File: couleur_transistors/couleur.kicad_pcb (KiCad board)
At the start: 2 copper layers, 13.7 x 33.5 mm, 12 parts, among them P1 CONN_02X03, P2 Mounting, U1 S4282-51

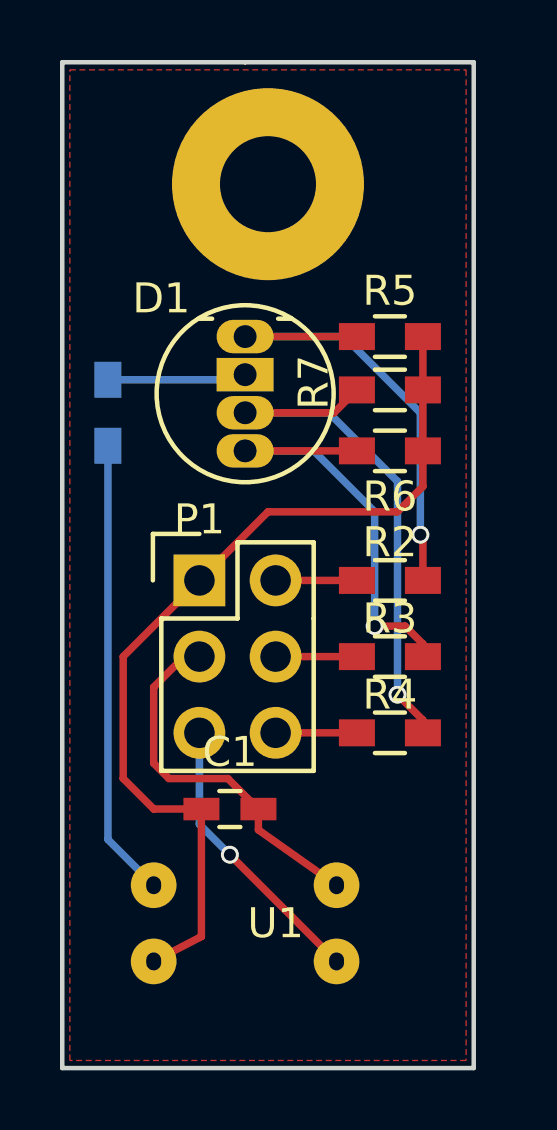
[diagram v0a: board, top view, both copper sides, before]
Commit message: COuleur avec transistors
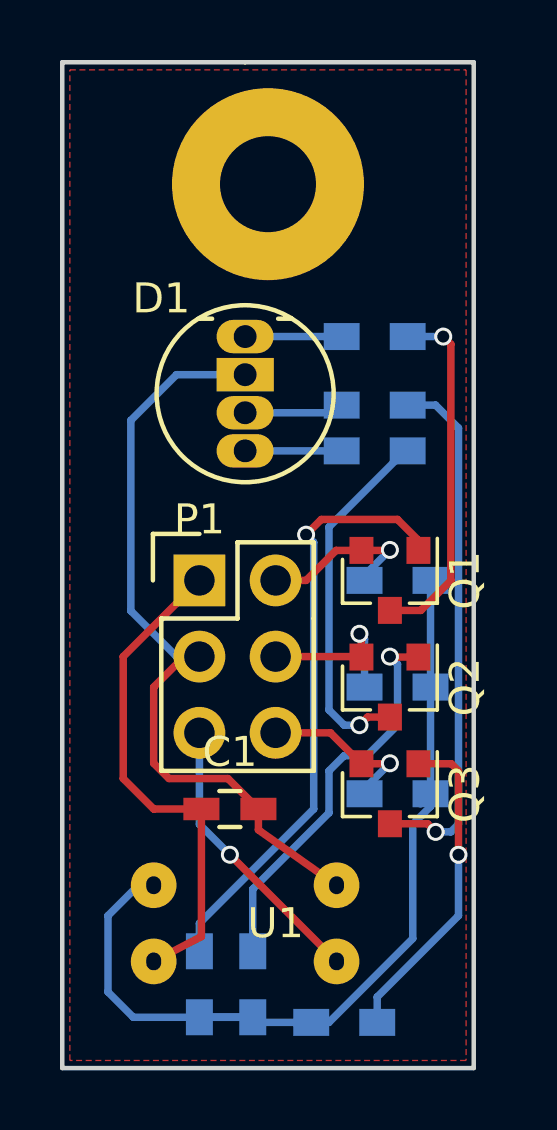
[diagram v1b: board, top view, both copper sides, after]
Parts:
- added Q1: Q_PNP_BEC, TO_SOT_Packages_SMD:SOT-23, F.Cu at (182.1, 104.1)
- added Q2: Q_PNP_BEC, TO_SOT_Packages_SMD:SOT-23, F.Cu at (182.1, 107.7)
- added Q3: Q_PNP_BEC, TO_SOT_Packages_SMD:SOT-23, F.Cu at (182.1, 111.3)
- added R8: 100, Resistors_SMD:R_0603_HandSoldering, B.Cu at (182.4, 111.3)
- added R9: 20, Resistors_SMD:R_0603_HandSoldering, B.Cu at (181.6, 98.3)
- R1: value R -> 0
- R2: value 150 -> 100; moved to B.Cu
- R3: value 76 -> 20; moved to B.Cu
- R4: value 82 -> 0; moved to B.Cu
- R5: value 600 -> 100; moved to B.Cu
- R6: value 122 -> 20; moved to B.Cu
- R7: value 131 -> 0; moved to B.Cu
- moved R7 21.1 mm to (180.6, 118.9), turned to 180 degrees
- moved R1 19.3 mm to (175.8, 117.6)
- moved R5 11.7 mm to (182.4, 107.7), turned to 180 degrees
- moved R3 10.7 mm to (181.6, 96.0), turned to 180 degrees
- moved R4 9.55 mm to (177.5, 117.6), turned to 270 degrees
- moved R6 0.51 mm to (181.6, 99.8), turned to 180 degrees
- moved R2 0.25 mm to (182.4, 104.1), turned to 180 degrees
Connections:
- D1 pad 2: Net-(D1-Pad2) -> GND
- R1 pad 1: Net-(D1-Pad2) -> Net-(Q1-Pad1)
- R1 pad 2: Net-(R1-Pad2) -> CATH
- R2 pad 1: RED -> CATH
- R2 pad 2: Net-(D1-Pad1) -> RED
- R3 pad 1: GREEN -> Net-(Q1-Pad3)
- R3 pad 2: Net-(D1-Pad4) -> Net-(D1-Pad1)
- R4 pad 1: BLUE -> Net-(Q2-Pad1)
- R4 pad 2: Net-(D1-Pad3) -> CATH
- R5 pad 1: Net-(D1-Pad1) -> CATH
- R5 pad 2: +5VL -> GREEN
- R6 pad 1: Net-(D1-Pad4) -> Net-(Q2-Pad3)
- R6 pad 2: +5VL -> Net-(D1-Pad4)
- R7 pad 1: Net-(D1-Pad3) -> Net-(Q3-Pad1)
- R7 pad 2: +5VL -> CATH
- U1 pad 1: Net-(R1-Pad2) -> CATH
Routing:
- net CATH: track 0.00 -> 31.3 mm
- net Net-(Q1-Pad1): track 0.00 -> 20.1 mm, vias 0 -> 1
- net Net-(Q3-Pad3): track 0.00 -> 17.7 mm, vias 0 -> 1
- net Net-(D1-Pad3): track 18.8 -> 3.32 mm, vias 1 -> 0
- net Net-(R1-Pad2): track 15.3 -> 0.00 mm
- net +5VL: track 30.5 -> 16.7 mm
- net GND: track 12.5 -> 26.2 mm
- net Net-(Q2-Pad1): track 0.00 -> 13.3 mm, vias 0 -> 1
- net Net-(D1-Pad1): track 16.2 -> 3.22 mm, vias 1 -> 0
- net Net-(Q2-Pad3): track 0.00 -> 12.1 mm, vias 0 -> 1
- net Net-(Q1-Pad3): track 0.00 -> 11.9 mm, vias 0 -> 1
- net Net-(D1-Pad4): track 15.2 -> 3.47 mm, vias 1 -> 0
- net Net-(Q3-Pad1): track 0.00 -> 10.9 mm, vias 0 -> 1
- net Net-(D1-Pad2): track 4.88 -> 0.00 mm
- net RED: track 2.79 -> 5.85 mm, vias 0 -> 1
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
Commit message: Couleur
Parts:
- removed Q2, Q3: Q_PNP_BEC, TO_SOT_Packages_SMD:SOT-23
- removed R1, R4, R7: 0, Resistors_SMD:R_0603_HandSoldering
- removed R2, R5, R8: 100, Resistors_SMD:R_0603_HandSoldering
- R3, R6, R9: moved to F.Cu
- moved Q1 7.41 mm to (182.2, 111.5), turned to 180 degrees
- moved R6 1.61 mm to (182.3, 101.2)
- moved R9 0.77 mm to (182.3, 98.5)
- moved R3 0.74 mm to (182.3, 96.0)
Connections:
- D1 pad 2: GND -> Net-(D1-Pad2)
- Q1 pad 1: Net-(Q1-Pad1) -> CATH
- Q1 pad 2: RED -> Net-(D1-Pad2)
- Q1 pad 3: Net-(Q1-Pad3) -> GND
- R3 pad 1: Net-(Q1-Pad3) -> RED
- R6 pad 1: Net-(Q2-Pad3) -> GREEN
- R9 pad 1: Net-(Q3-Pad3) -> BLUE
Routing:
- net CATH: track 31.3 -> 10.6 mm, vias 0 -> 2
- net Net-(Q1-Pad1): track 20.1 -> 0.00 mm, vias 1 -> 0
- net Net-(Q3-Pad3): track 17.7 -> 0.00 mm, vias 1 -> 0
- net Net-(D1-Pad2): track 0.00 -> 16.0 mm
- net Net-(Q2-Pad1): track 13.3 -> 0.00 mm, vias 1 -> 0
- net Net-(Q2-Pad3): track 12.1 -> 0.00 mm, vias 1 -> 0
- net Net-(Q1-Pad3): track 11.9 -> 0.00 mm, vias 1 -> 0
- net Net-(Q3-Pad1): track 10.9 -> 0.00 mm, vias 1 -> 0
- net GND: track 26.2 -> 15.7 mm
- net BLUE: track 5.61 -> 14.3 mm
- net RED: track 5.85 -> 11.0 mm
- net GREEN: track 5.53 -> 9.82 mm
- net Net-(D1-Pad4): track 3.47 -> 5.02 mm, vias 0 -> 1
- net Net-(D1-Pad1): track 3.22 -> 3.98 mm, vias 0 -> 1
- net Net-(D1-Pad3): track 3.32 -> 4.05 mm, vias 0 -> 1
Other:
- board text added: "R G B"
- board text removed: "B"
- board text removed: "G"
- board text removed: "R"

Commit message: maj
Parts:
- removed Q1: Q_PNP_BEC, TO_SOT_Packages_SMD:SOT-23
- removed R6, R9: 20, Resistors_SMD:R_0603_HandSoldering
- added C2: 1uF, Capacitors_SMD:C_0603_HandSoldering, F.Cu at (182.2, 94.2)
- added C3: 1uF, Capacitors_SMD:C_0603_HandSoldering, F.Cu at (182.3, 100.0)
- added C4: 1uF, Capacitors_SMD:C_0603_HandSoldering, F.Cu at (182.3, 98.5)
- added C5: 1uF, Capacitors_SMD:C_0603_HandSoldering, F.Cu at (182.5, 108.8)
- added R1: 20, Resistors_SMD:R_0603_HandSoldering, F.Cu at (172.5, 95.9)
- added R2: 20, Resistors_SMD:R_0603_HandSoldering, F.Cu at (172.5, 100.8)
- added U2: NLAS2066, Housings_SSOP:TSSOP-8_3x3mm_Pitch0.65mm, B.Cu at (182.6, 103.4)
- added U3: NLAS2066, Housings_SSOP:TSSOP-8_3x3mm_Pitch0.65mm, B.Cu at (182.6, 109.4)
- R3: moved to B.Cu
- moved R3 10.5 mm to (172.5, 99.8), turned to 270 degrees
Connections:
- D1 pad 1: Net-(D1-Pad1) -> Net-(C2-Pad2)
- D1 pad 2: Net-(D1-Pad2) -> CATH
- D1 pad 3: Net-(D1-Pad3) -> Net-(C4-Pad2)
- R3 pad 1: RED -> Net-(C4-Pad2)
- R3 pad 2: Net-(D1-Pad1) -> Net-(R3-Pad2)
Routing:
- net +5VL: track 16.7 -> 53.2 mm, vias 0 -> 2
- net GND: track 15.7 -> 43.2 mm, vias 0 -> 2
- net Net-(R3-Pad2): track 0.00 -> 16.1 mm
- net Net-(D1-Pad2): track 16.0 -> 0.00 mm
- net Net-(R1-Pad1): track 0.00 -> 14.0 mm, vias 0 -> 1
- net Net-(R2-Pad2): track 0.00 -> 13.7 mm, vias 0 -> 1
- net CATH: track 10.6 -> 20.7 mm, vias 2 -> 1
- net Net-(C2-Pad2): track 0.00 -> 9.89 mm
- net Net-(C4-Pad2): track 0.00 -> 8.96 mm, vias 0 -> 1
- net BLUE: track 14.3 -> 6.75 mm, vias 1 -> 0
- net RED: track 11.0 -> 5.31 mm
- net Net-(D1-Pad3): track 4.05 -> 0.00 mm, vias 1 -> 0
- net Net-(D1-Pad1): track 3.98 -> 0.00 mm, vias 1 -> 0
- net Net-(C3-Pad1): track 5.02 -> 8.95 mm, vias 1 -> 0
